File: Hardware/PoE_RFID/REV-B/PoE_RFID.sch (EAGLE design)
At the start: 97 parts, among them IC2 ATMEGA32U4-MU, J6 10103594-0001LF, SW1 SPST_TACT-KMR2, U1 PN532, U2 SPX3819-3.3, U3 74AHC1G125, U4 W5500, X2 J1011FHANRUN, Y1 27.12MHz, Y4 8MHz

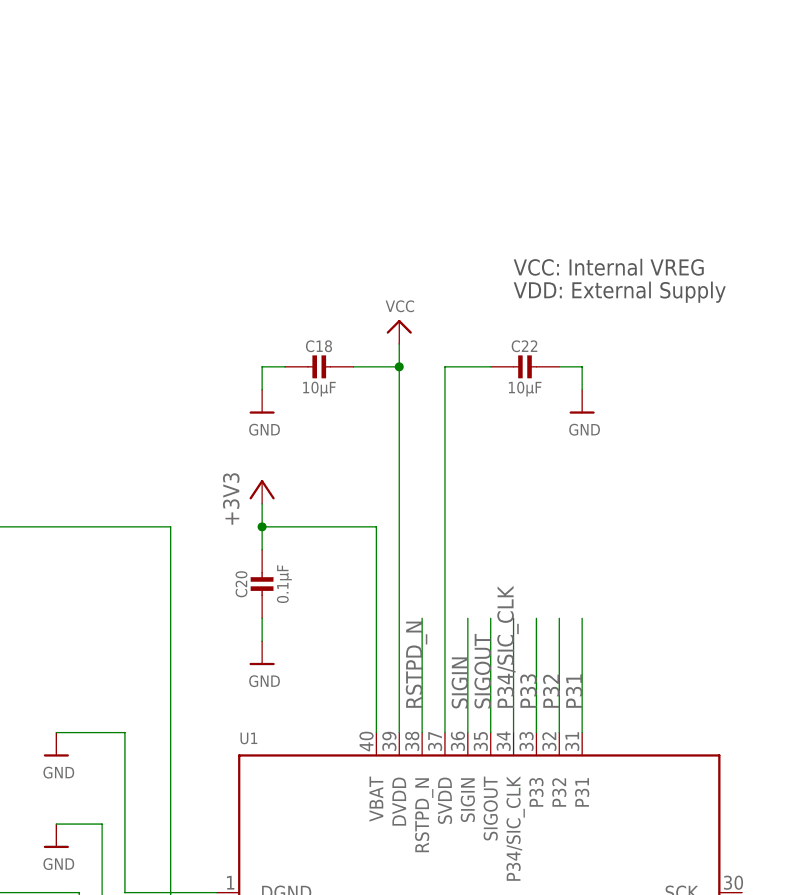
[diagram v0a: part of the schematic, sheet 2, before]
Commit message: HEEP-615 added reset pulllup
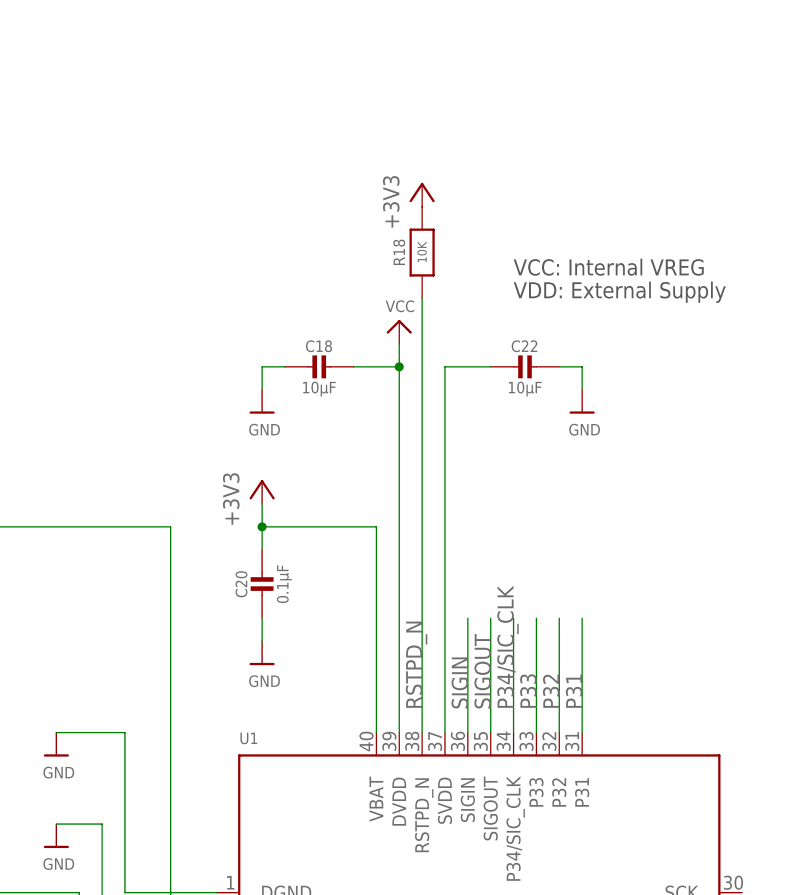
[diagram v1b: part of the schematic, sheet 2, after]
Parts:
- added R18: 10K, microbuilder:RESISTOR_0603_NOOUT
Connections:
- net +3V3: now also R18.2
- net RSTPD_N: now also R18.1
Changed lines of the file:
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@@
 <?xml version="1.0" encoding="utf-8"?>
 <!DOCTYPE eagle SYSTEM "eagle.dtd">
-<eagle version="8.4.3">
+<eagle version="8.5.0">
 <drawing>
 <settings>
@@
 <part name="GND5" library="supply1" deviceset="GND" device=""/>
 <part name="+3V13" library="supply1" deviceset="+3V3" device=""/>
+<part name="R18" library="microbuilder" deviceset="RESISTOR" device="_0603_NOOUT" value="10K"/>
+<part name="+3V14" library="supply1" library_urn="urn:adsk.eagle:library:371" deviceset="+3V3" device=""/>
 </parts>
 <sheets>
@@
 <instance part="+3V12" gate="G$1" x="162.56" y="203.2"/>
 <instance part="+3V11" gate="G$1" x="83.82" y="66.04"/>
+<instance part="R18" gate="G$1" x="180.34" y="228.6" rot="R90"/>
+<instance part="+3V14" gate="G$1" x="180.34" y="236.22"/>
 </instances>
 <busses>
@@
 <net name="RSTPD_N" class="0">
 <segment>
-<wire x1="180.34" y1="175.26" x2="180.34" y2="187.96" width="0.1524" layer="91"/>
 <label x="180.34" y="177.8" size="1.778" layer="95" rot="R90"/>
 <pinref part="U1" gate="G$1" pin="RSTPD_N"/>
+<pinref part="R18" gate="G$1" pin="1"/>
+<wire x1="180.34" y1="223.52" x2="180.34" y2="175.26" width="0.1524" layer="91"/>
 </segment>
 </net>
@@
 <pinref part="+3V11" gate="G$1" pin="+3V3"/>
 </segment>
-</net>
+<segment>
+<pinref part="R18" gate="G$1" pin="2"/>
+<pinref part="+3V14" gate="G$1" pin="+3V3"/>
+</segment>
+</net>

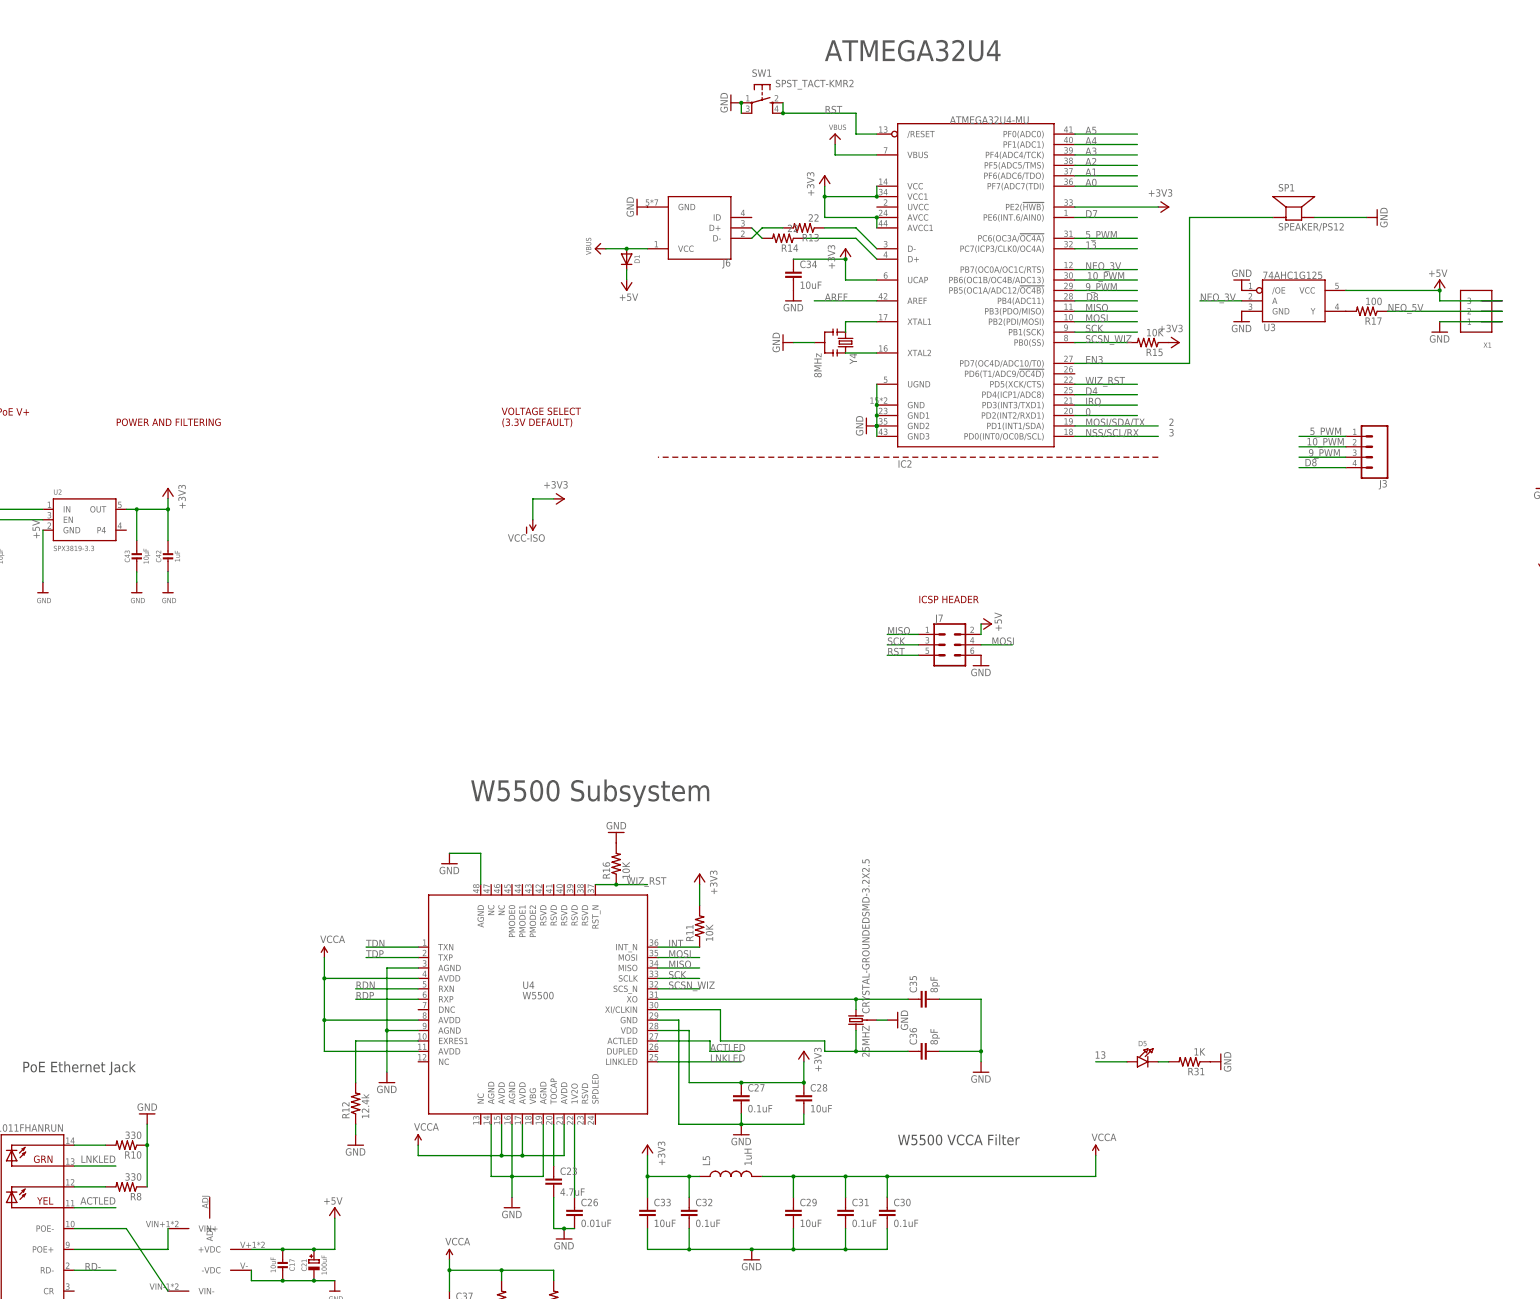
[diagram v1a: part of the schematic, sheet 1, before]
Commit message: HEEP-615 added eagle backup files to gitignore, added pin 1 indicator to PoE module. more progress on RFID pcb layout
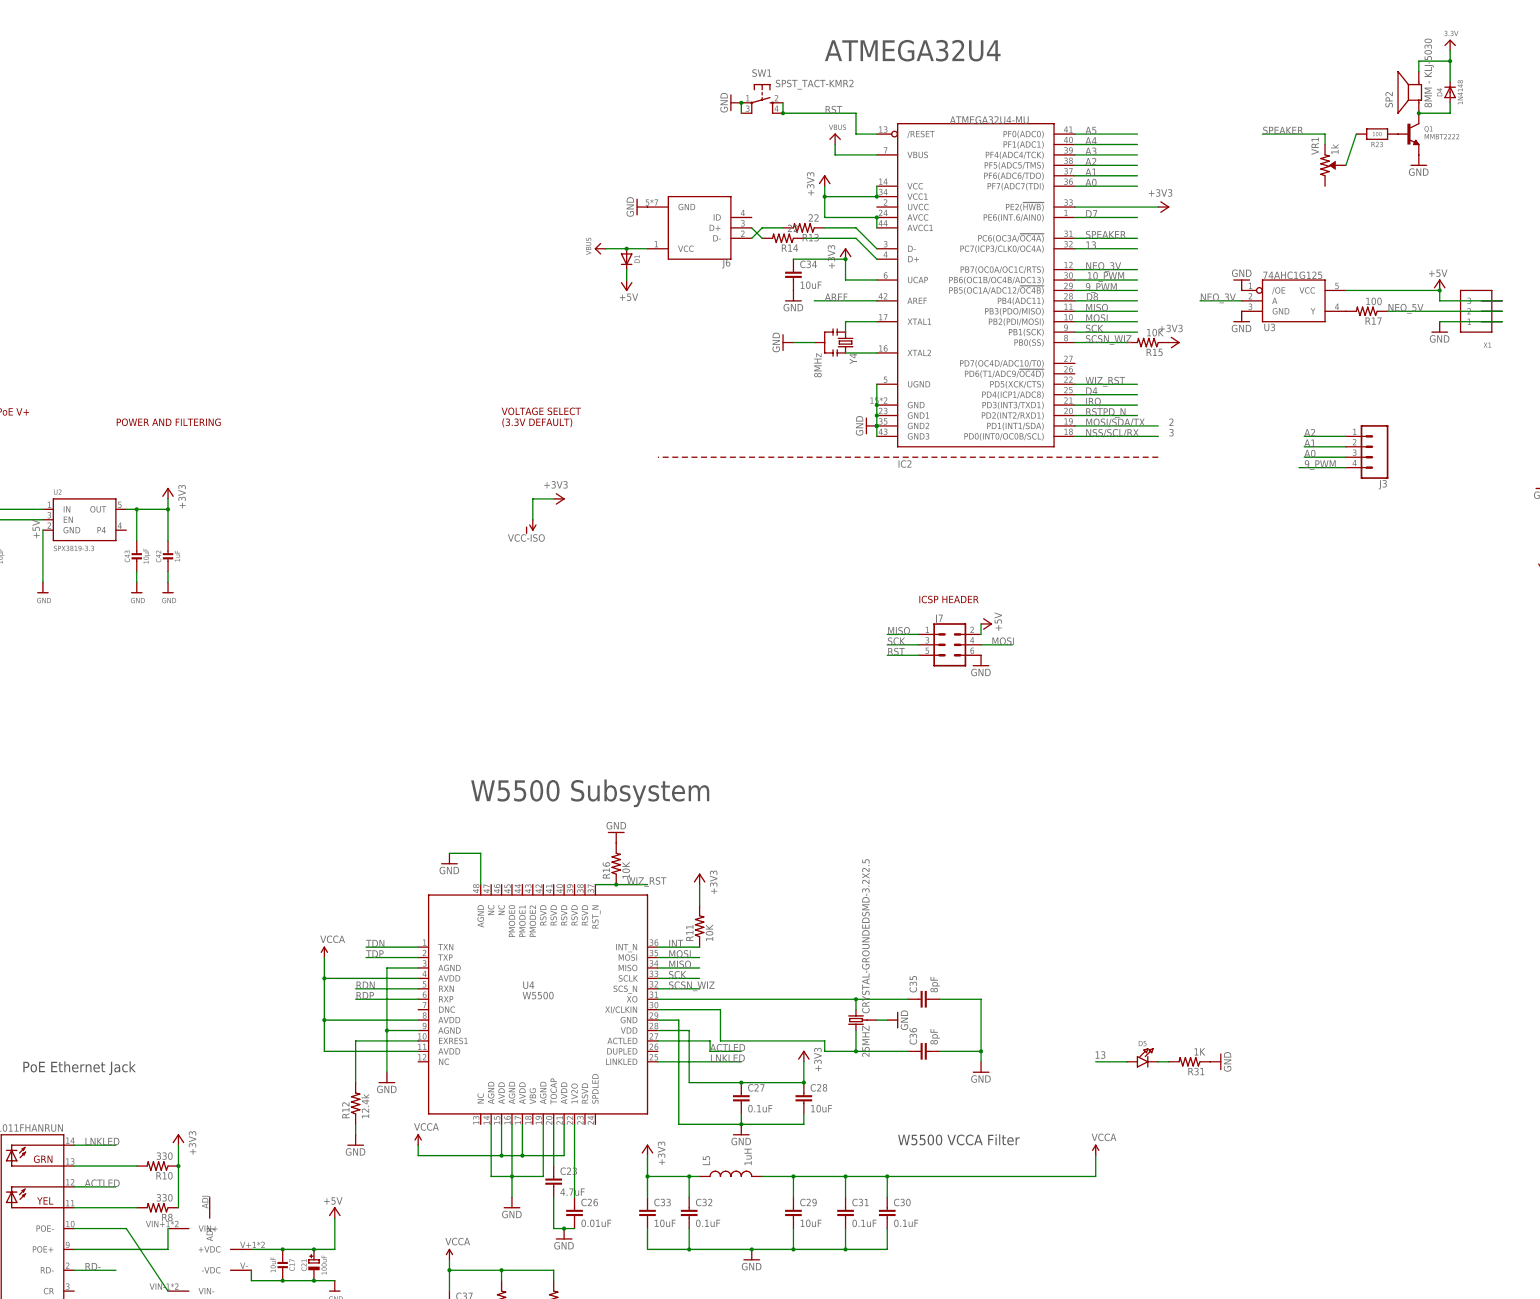
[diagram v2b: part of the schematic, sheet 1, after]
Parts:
- removed SP1: SPEAKER/PS12, microbuilder:SPEAKER/PS12
- added D4: 1N4148, microbuilder:DIODESOD-323
- added Q1: MMBT2222, microbuilder:TRANSISTOR_NPNWIDE
- added R23: 100, microbuilder:RESISTOR_0603_NOOUT
- added SP2: 8MM - KLJ-5030, microbuilder:SPEAKER_BUZZER5MM
- added VR1: 1k, SparkFun-Resistors:TRIMPOT-SMD-3MM-OPEN-1/10W-25%
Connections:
- removed net 0: IC2.PD2(INT2/RXD1)
- removed net 5_PWM: IC2.PC6(OC3A/!OC4A), J3.1
- removed net EN3: IC2.PD7(OC4D/ADC10/T0), SP1.+
- new net 3.3V: D4.C, SP2.-
- new net N$29: Q1.B, R23.1
- new net N$30: D4.A, Q1.C, SP2.+
- new net N$31: R23.2, VR1.WIPER
- new net SPEAKER: IC2.PC6(OC3A/!OC4A), VR1.CCW
- net +3V3: now also R10.1, R8.1
- net 10_PWM: no longer J3.2
- net 9_PWM: now also J3.4; no longer J3.3
- net A0: now also J3.3
- net A1: now also J3.2
- net A2: now also J3.1
- net ACTLED: now also X2.YEL-C; no longer X2.YEL-A
- net D8: no longer J3.4
- net GND: now also Q1.E; no longer R10.1, R8.1, SP1.-
- net LNKLED: now also X2.GRN-C; no longer X2.GRN-A
- net N$27: now also R8.2, X2.YEL-A; no longer R10.2, X2.GRN-C
- net N$28: now also R10.2, X2.GRN-A; no longer R8.2, X2.YEL-C
- net RSTPD_N: now also IC2.PD2(INT2/RXD1)
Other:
- moved on the sheet: R10, R8

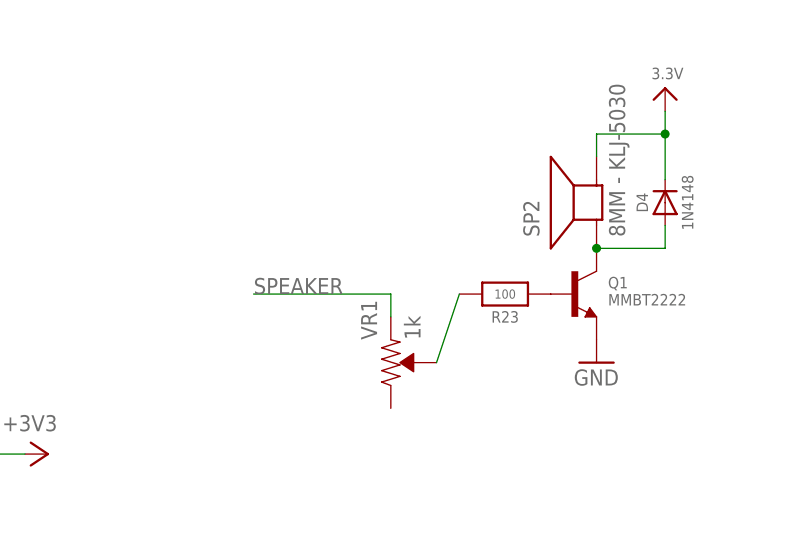
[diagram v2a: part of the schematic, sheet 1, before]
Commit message: HEEP-615 shrunk microusb holes to prevent wiggle. PCB for dylan to review
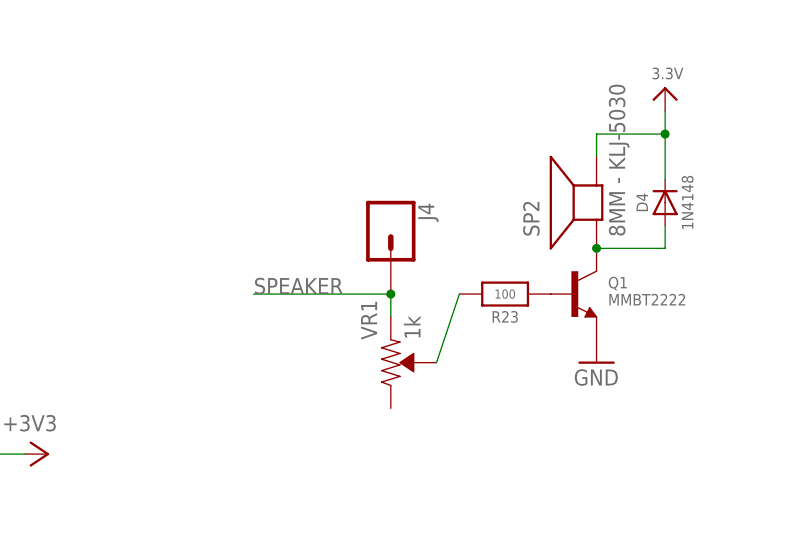
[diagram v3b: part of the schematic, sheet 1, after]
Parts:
- added J4: (no value), SparkFun-Connectors:CONN_01
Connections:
- net SPEAKER: now also J4.1
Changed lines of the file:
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@@
 <part name="+3V15" library="supply1" deviceset="+3V3" device=""/>
 <part name="VR1" library="SparkFun-Resistors" deviceset="TRIMPOT" device="-SMD-3MM-OPEN-1/10W-25%" value="1k"/>
+<part name="J4" library="SparkFun-Connectors" deviceset="CONN_01" device=""/>
 </parts>
 <sheets>
@@
 <instance part="+3V15" gate="G$1" x="71.12" y="88.9" rot="MR0"/>
 <instance part="VR1" gate="R?" x="350.52" y="325.12"/>
+<instance part="J4" gate="G$1" x="350.52" y="340.36" rot="R270"/>
 </instances>
 <busses>
@@
 <pinref part="VR1" gate="R?" pin="CCW"/>
 <wire x1="350.52" y1="330.2" x2="350.52" y2="332.74" width="0.1524" layer="91"/>
-</segment>
-<segment>
+<pinref part="J4" gate="G$1" pin="1"/>
+<junction x="350.52" y="332.74"/>
+</segment>
+<segment>

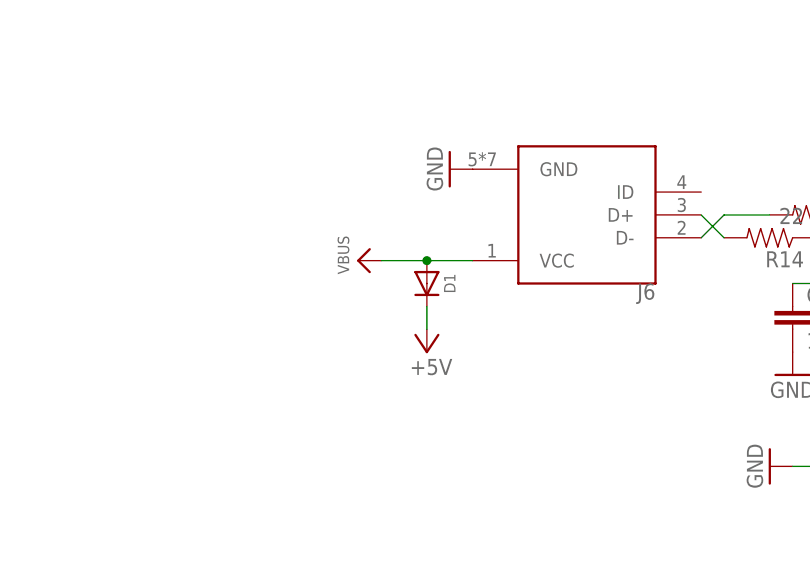
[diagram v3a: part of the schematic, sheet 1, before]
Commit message: HEEP-651 updated capacitor voltage ratings to reflect true minimum requirements
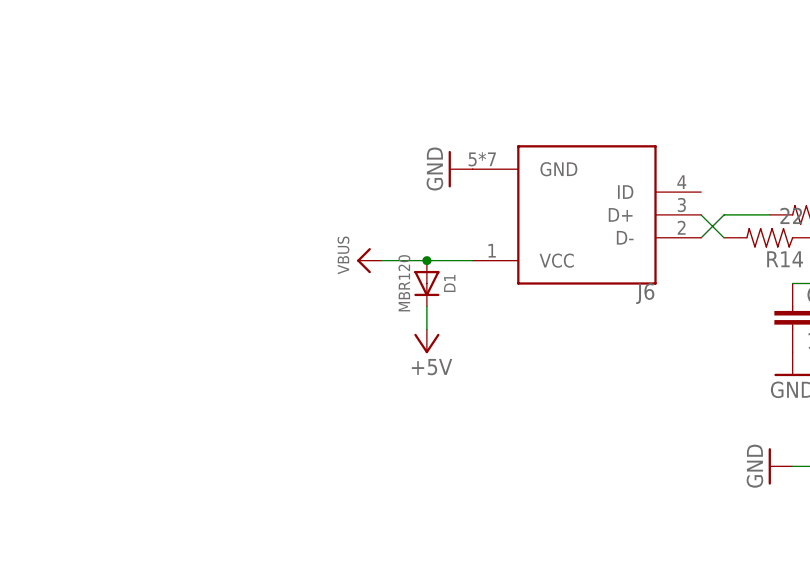
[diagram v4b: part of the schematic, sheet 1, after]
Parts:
- D1: value (none) -> MBR120
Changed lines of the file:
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@@
 <part name="P+2" library="microbuilder" deviceset="VCC" device=""/>
 <part name="P+3" library="microbuilder" deviceset="VCC" device=""/>
-<part name="D1" library="microbuilder" deviceset="DIODE" device="SOD-123"/>
+<part name="D1" library="microbuilder" deviceset="DIODE" device="SOD-123" value="MBR120"/>
 <part name="P+5" library="supply1" deviceset="+5V" device=""/>
 <part name="P+6" library="supply1" deviceset="+5V" device=""/>
